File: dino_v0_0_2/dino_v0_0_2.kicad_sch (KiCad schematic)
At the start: 13 parts, among them U23 74LS04, U6 74LS163, U7 74LS138, U8 74LS138

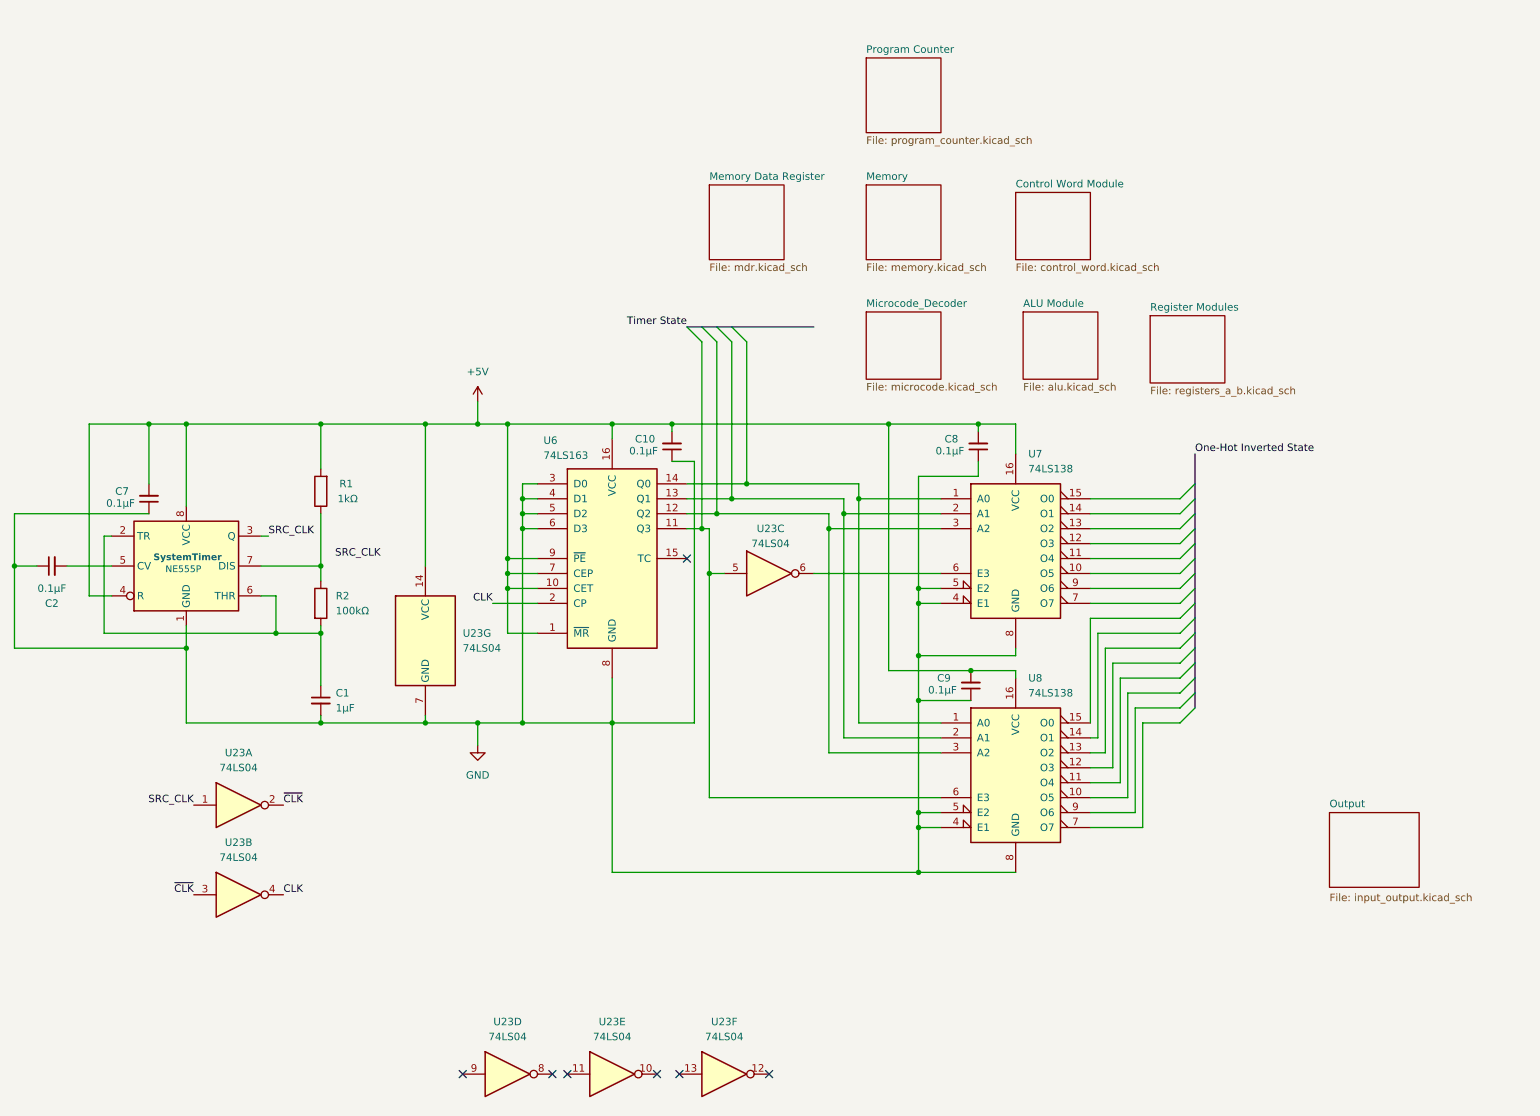
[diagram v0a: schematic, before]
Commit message: DINO v0.0.3: complete ALU/control-word, add MAR+reset sheets, wire reset circuit
ALU sheet: flags register moved from '173 (not in stock) to '273 + a '157
mux to emulate the missing load-enable pins; Z-detect built from a NOR+AND
De Morgan tree instead of a '260; ALU_CIN built from NAND(SA1,SA0) reusing
two already-placed spare gates instead of a dedicated XOR/'86. Sheet is
now fully wired and netlist-clean.

Control word sheet: all 16 CW bits assigned and wired (3x '138 decoders
for the load/source/misc fields, direct bus taps for HALT/PC_MAR_MUX/
PC_UP/END and the ALU SA[2:0] select). Found and fixed several cross-
sheet signal-name mismatches this uncovered (OUT_REG_LOAD/REG_OUT_LOAD,
PC_MAR_MUX/PC_MUX, T-state counter labels, a mirror-reversed IRB->ROM-
address buffer in microcode).

New: MAR and reset sheets, wired into the root hierarchy. Reset circuit
is a from-scratch design: RC+button+74HC14 Schmitt front end feeds the
async PRESET of the clock cluster's spare '74 half (U27B), synchronizing
release to CLK; its Q/~Q fan out to the flags register, the T-state
counter's clear, and (OR'd with the existing microcode-driven PC_CLEAR,
reusing spare gates on the same '02) the PC counters' clear.

Deprecated 7 schematic files no longer referenced by the root sheet's
hierarchy into dino_v0_0_2/deprecated/. Added docs/notes/kicad_netlist.py,
a .kicad_sch connectivity auditor (pin/net resolution incl. buses and
same-name local-label merging) used throughout this session to find the
above bugs; archived completed-work docs into docs/notes/Done/ and
rewrote dino_session_state.md as the current authoritative state+TODO.

Co-Authored-By: Claude Sonnet 5 <noreply@anthropic.com>
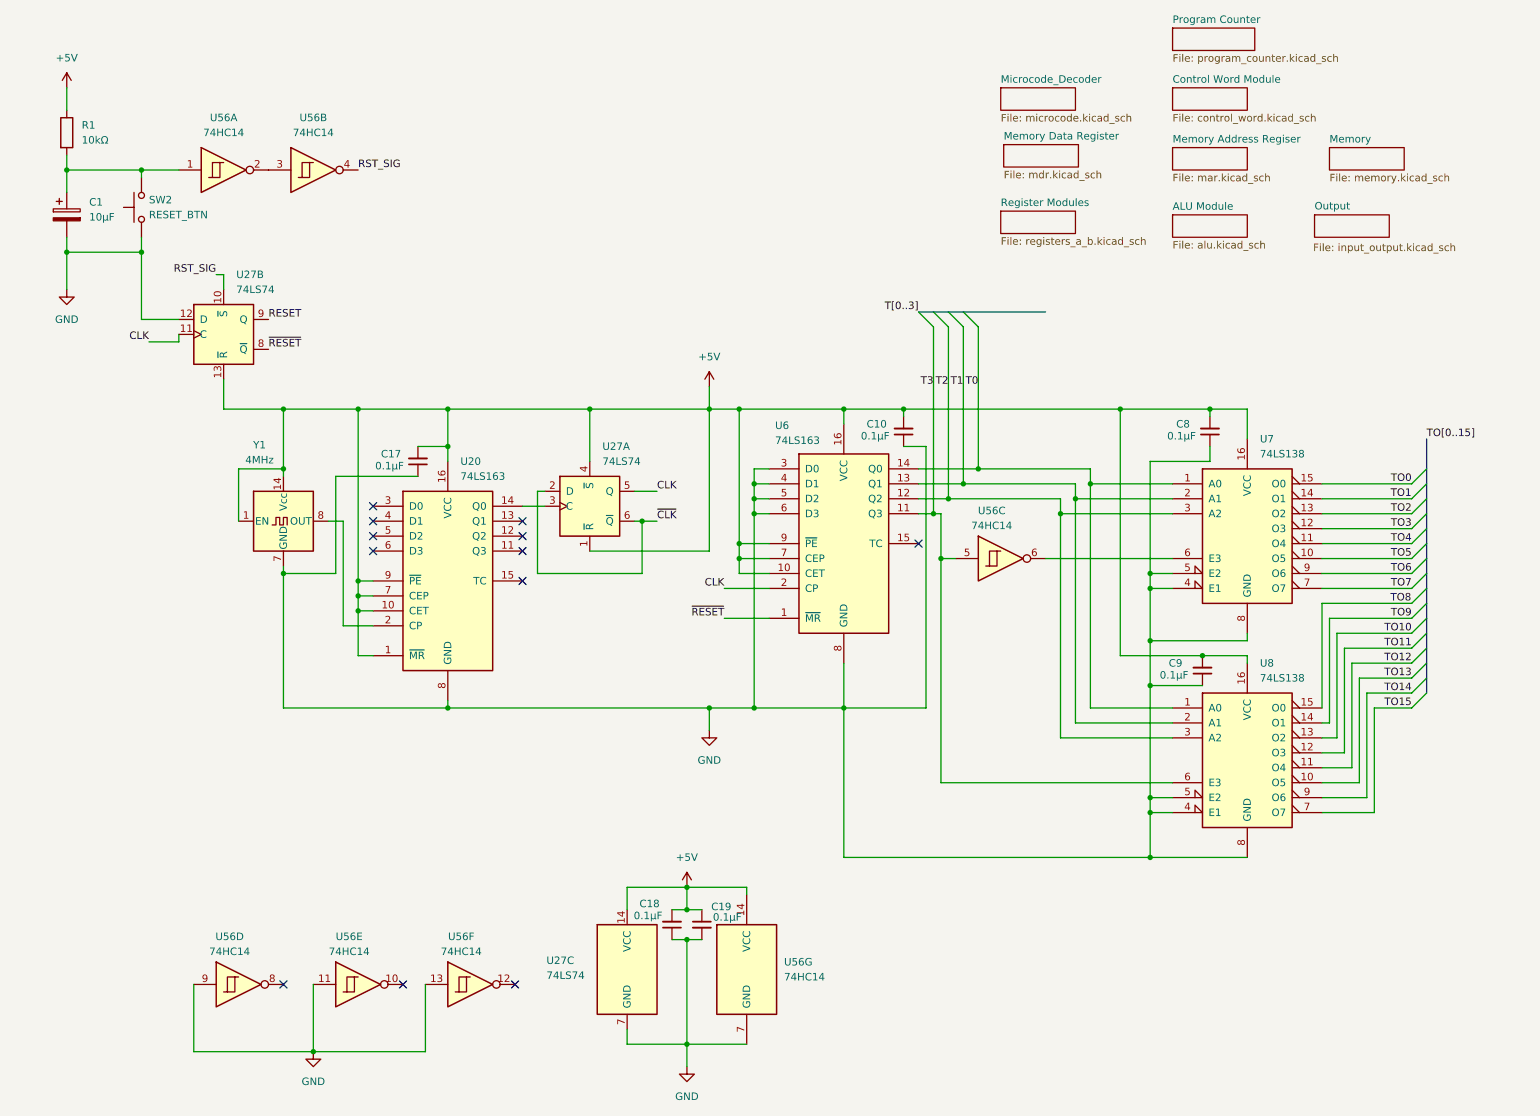
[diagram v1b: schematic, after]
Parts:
- removed C1: 1µF, symbol Device:C_Small
- removed C2, C7: 0.1µF, symbol Device:C_Small
- removed R2: 100kΩ, symbol Device:R
- removed SystemTimer: NE555P, Package_DIP:DIP-8_W7.62mm, symbol Timer:NE555P
- removed U23: 74LS04, symbol 74xx:74LS04
- added C1: 10µF, symbol Device:C_Polarized
- added C17, C18, C19: 0.1µF, symbol Device:C_Small
- added SW2: RESET_BTN, symbol Switch:SW_Push
- added U20: 74LS163, symbol 74xx:74LS163
- added U27: 74LS74, symbol 74xx:74LS74
- added U56: 74HC14, symbol 74xx:74HC14
- added Y1: 4MHz, Oscillator:Oscillator_DIP-14, symbol Oscillator:CXO_DIP14
- R1: value 1kΩ -> 10kΩ
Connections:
- net +5V: now also R1.1, C17.2, C18.2, C19.1, U20.1 (~{MR}), U20.10 (CET), U20.16 (VCC), U20.7 (CEP), U20.9 (~{PE}), U27.1 (~{R}), U27.13 (~{R}), U27.14 (VCC), U27.4 (~{S}), U56.14 (VCC), Y1.1 (EN), Y1.14 (Vcc); no longer R1.2, U6.1 (~{MR})
- net CLK: now also U27.11 (C), U27.5 (Q)
- net GND: now also C1.2, C17.1, C18.1, C19.2, SW2.1, U20.8 (GND), U27.12 (D), U27.7 (GND), U56.11, U56.13, U56.7 (GND), U56.9, Y1.7 (GND)
- net ~{CLK}: now also U27.2 (D), U27.6 (~{Q})
- net T0: now reaches U6.14 (Q0), U7.1 (A0), U8.1 (A0)
- net TO5: now reaches U7.10 (O5)
- net TO4: now reaches U7.11 (O4)
- net TO3: now reaches U7.12 (O3)
- net TO2: now reaches U7.13 (O2)
- net TO1: now reaches U7.14 (O1)
- net TO0: now reaches U7.15 (O0)
- net T1: now reaches U6.13 (Q1), U7.2 (A1), U8.2 (A1)
- net T2: now reaches U6.12 (Q2), U7.3 (A2), U8.3 (A2)
- net at U7.6 (E3): now also U56.6
- net TO7: now reaches U7.7 (O7)
- net TO6: now reaches U7.9 (O6)
- net T3: now reaches U6.11 (Q3), U8.6 (E3)
- net T3: now also U56.5
- net TO13: now reaches U8.10 (O5)
- net TO12: now reaches U8.11 (O4)
- net TO11: now reaches U8.12 (O3)
- net TO10: now reaches U8.13 (O2)
- net TO9: now reaches U8.14 (O1)
- net TO8: now reaches U8.15 (O0)
- net TO15: now reaches U8.7 (O7)
- net TO14: now reaches U8.9 (O6)
- new net: C1.1, R1.2, SW2.2, U56.1
- new net: U56.2, U56.3
- new net: U20.2 (CP), Y1.8 (OUT)
- new net: U20.14 (Q0), U27.3 (C)
- new net RESET: U27.9 (Q)
- new net RST_SIG: U27.10 (~{S}), U56.4
- new net ~{RESET}: U27.8 (~{Q}), U6.1 (~{MR})
- no-connect marks 7 -> 12
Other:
- added sheet Memory Address Regiser (mar.kicad_sch)
- moved on the sheet: C10, C8, C9, U6, U7, U8
